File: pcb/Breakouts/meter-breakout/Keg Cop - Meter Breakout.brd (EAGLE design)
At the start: 44.7 x 33.9 mm, 4 parts

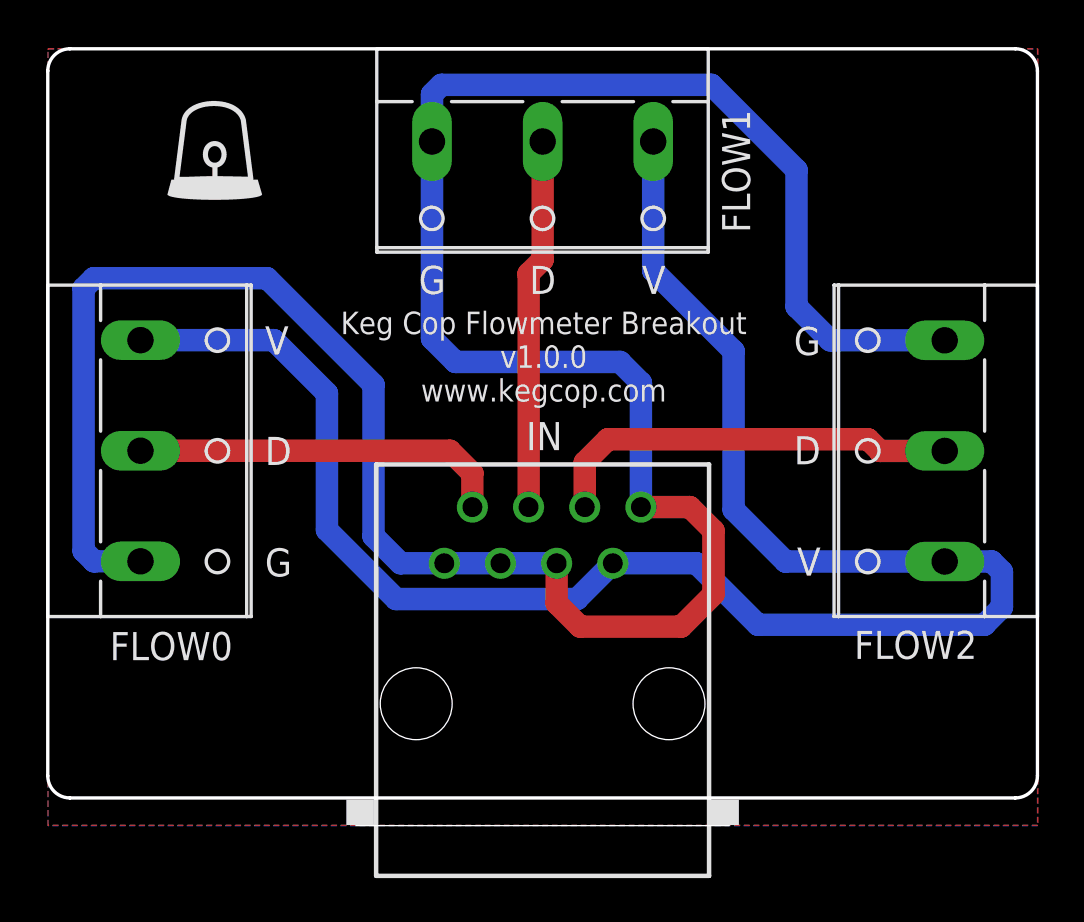
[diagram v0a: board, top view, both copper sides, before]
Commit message: Add ground pour vias
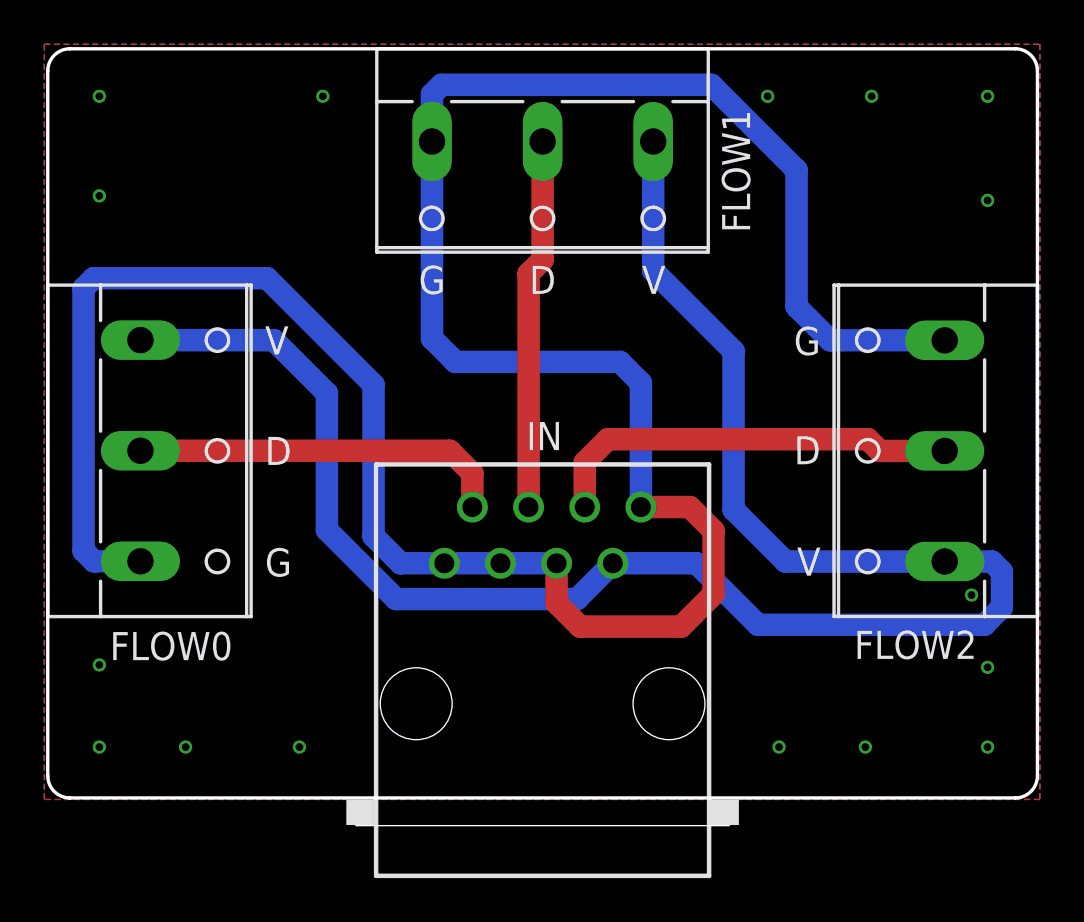
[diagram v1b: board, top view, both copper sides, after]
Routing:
- net GND: vias 0 -> 16
